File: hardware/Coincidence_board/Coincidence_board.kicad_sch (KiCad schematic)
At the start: 68 parts, among them J1 Inputs, J3 POWER_IN, J4 Morpho_Gauche, J7 Morpho_Droite, SW1 SW_1, U1 74HCT74, U2 74HCT74, U3 LM7805_TO220, U4 74HC74, U5 74HC74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

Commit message: Update Coincidence Board / Dephi 2024
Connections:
- net A2out_nuc: now also J7.29 (Pin_29); no longer J7.5 (Pin_5)
- net AB2out_nuc: now also J7.5 (Pin_5); no longer J7.32 (Pin_32)
- net ABCout_nuc: now also J7.33 (Pin_33); no longer J7.13 (Pin_13)
- net AC2out_nuc: now also J4.37 (Pin_37); no longer J7.26 (Pin_26)
- net B2out_nuc: now also J4.15 (Pin_15); no longer J7.7 (Pin_7)
- net BC2out_nuc: now also J4.3 (Pin_3); no longer J7.31 (Pin_31)
- net C2out_nuc: now also J4.40 (Pin_40)
- net GND: now also U1.2 (D)
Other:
- note added: "PB_4"
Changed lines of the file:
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@@
 	(wire
 		(pts
+			(xy 90.17 185.42) (xy 91.44 185.42)
+		)
+		(stroke
+			(width 0)
+			(type default)
+		)
+	)
+	(wire
+		(pts
 			(xy 49.53 170.18) (xy 52.07 170.18)
 		)
@@
 	(wire
 		(pts
+			(xy 90.17 180.34) (xy 91.44 180.34)
+		)
+		(stroke
+			(width 0)
+			(type default)
+		)
+	)
+	(wire
+		(pts
 			(xy 68.58 73.66) (xy 68.58 74.93)
 		)
@@
 	(wire
 		(pts
+			(xy 128.27 30.48) (xy 130.81 30.48)
+		)
+		(stroke
+			(width 0)
+			(type default)
+		)
+	)
+	(wire
+		(pts
 			(xy 264.16 83.82) (xy 265.43 83.82)
 		)
@@
 	(text "PB_8"
 		(exclude_from_sim no)
-		(at 75.692 149.86 0)
+		(at 74.168 150.114 0)
 		(effects
 			(font
@@
 	(text "PB_0"
 		(exclude_from_sim no)
-		(at 70.866 188.214 0)
+		(at 64.77 187.706 0)
 		(effects
 			(font
@@
 	(text "PB_9"
 		(exclude_from_sim no)
-		(at 75.692 152.654 0)
+		(at 74.168 152.654 0)
 		(effects
 			(font
@@
 	(text "PC_1"
 		(exclude_from_sim no)
-		(at 70.866 191.008 0)
+		(at 64.77 190.5 0)
 		(effects
 			(font
@@
 	(text "PC_0"
 		(exclude_from_sim no)
-		(at 70.866 193.548 0)
+		(at 64.77 193.04 0)
 		(effects
 			(font
@@
 		)
 	)
+	(text "PB_4"
+		(exclude_from_sim no)
+		(at 73.914 180.594 0)
+		(effects
+			(font
+				(size 1.27 1.27)
+			)
+		)
+	)
 	(text "PA_0"
 		(exclude_from_sim no)
@@
 	(global_label "C2out_nuc"
 		(shape input)
-		(at 105.41 160.02 0)
+		(at 49.53 193.04 0)
 		(fields_autoplaced yes)
 		(effects
@@
 		)
 		(property "Intersheetrefs" "${INTERSHEET_REFS}"
-			(at 117.5984 160.02 0)
+			(at 61.7184 193.04 0)
 			(effects
 				(font
@@
 	(global_label "BC2out_nuc"
 		(shape input)
-		(at 90.17 182.88 180)
+		(at 36.83 147.32 180)
 		(fields_autoplaced yes)
 		(effects
@@
 		)
 		(property "Intersheetrefs" "${INTERSHEET_REFS}"
-			(at 76.7116 182.88 0)
+			(at 23.3716 147.32 0)
 			(effects
 				(font
@@
 	(global_label "ABCout_nuc"
 		(shape input)
-		(at 90.17 160.02 180)
+		(at 90.17 185.42 180)
 		(fields_autoplaced yes)
 		(effects
@@
 		)
 		(property "Intersheetrefs" "${INTERSHEET_REFS}"
-			(at 76.8325 160.02 0)
+			(at 76.8325 185.42 0)
 			(effects
 				(font
@@
 	(global_label "AB2out_nuc"
 		(shape input)
-		(at 105.41 182.88 0)
+		(at 90.17 149.86 180)
 		(fields_autoplaced yes)
 		(effects
@@
 				(size 1.27 1.27)
 			)
-			(justify left)
+			(justify right)
 		)
 		(property "Intersheetrefs" "${INTERSHEET_REFS}"
-			(at 118.687 182.88 0)
+			(at 76.893 149.86 0)
 			(effects
 				(font
 					(size 1.27 1.27)
 				)
-				(justify left)
+				(justify right)
 				(hide yes)
 			)
@@
 	(global_label "B2out_nuc"
 		(shape input)
-		(at 90.17 152.4 180)
+		(at 36.83 162.56 180)
 		(fields_autoplaced yes)
 		(effects
@@
 		)
 		(property "Intersheetrefs" "${INTERSHEET_REFS}"
-			(at 77.9816 152.4 0)
+			(at 24.6416 162.56 0)
 			(effects
 				(font
@@
 	(global_label "A2out_nuc"
 		(shape input)
-		(at 90.17 149.86 180)
+		(at 90.17 180.34 180)
 		(fields_autoplaced yes)
 		(effects
@@
 		)
 		(property "Intersheetrefs" "${INTERSHEET_REFS}"
-			(at 78.163 149.86 0)
+			(at 78.163 180.34 0)
 			(effects
 				(font
@@
 	(global_label "AC2out_nuc"
 		(shape input)
-		(at 105.41 175.26 0)
+		(at 36.83 190.5 180)
 		(fields_autoplaced yes)
 		(effects
@@
 				(size 1.27 1.27)
 			)
-			(justify left)
+			(justify right)
 		)
 		(property "Intersheetrefs" "${INTERSHEET_REFS}"
-			(at 118.687 175.26 0)
+			(at 23.553 190.5 0)
 			(effects
 				(font
 					(size 1.27 1.27)
 				)
-				(justify left)
+				(justify right)
 				(hide yes)
 			)

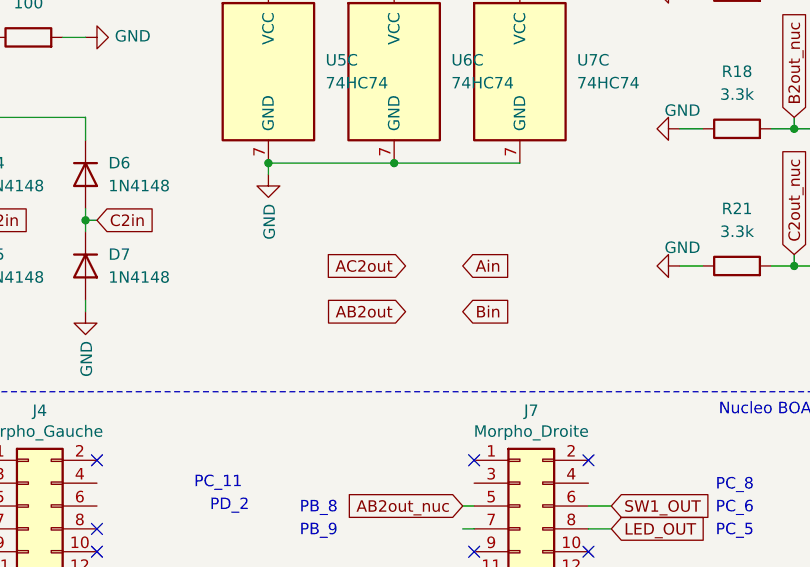
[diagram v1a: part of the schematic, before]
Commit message: Update Schematics of Electronic Board
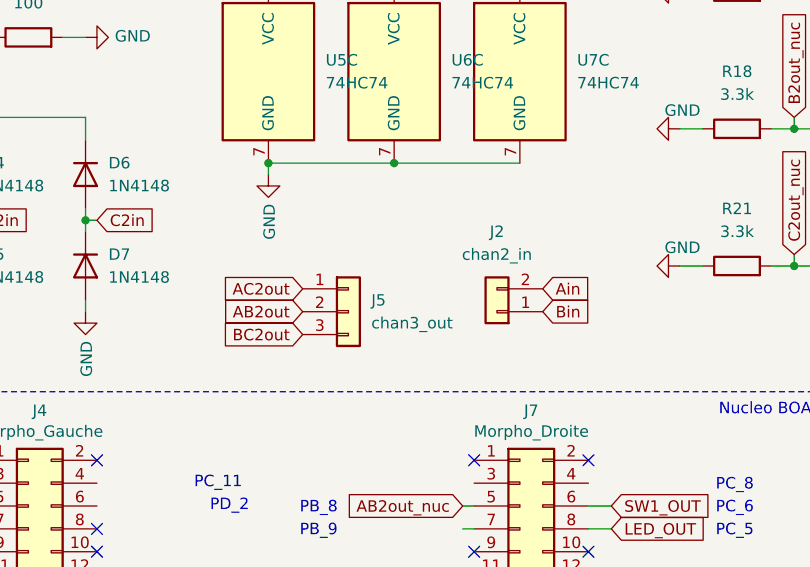
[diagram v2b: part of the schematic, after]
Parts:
- added J2: chan2_in, Connector_PinHeader_2.54mm:PinHeader_1x02_P2.54mm_Vertical, symbol Connector_Generic:Conn_01x02
- added J5: chan3_out, Connector_PinHeader_2.54mm:PinHeader_1x03_P2.54mm_Vertical, symbol Connector_Generic:Conn_01x03
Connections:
- net AB2out: now also J5.2 (Pin_2)
- net AC2out: now also J5.1 (Pin_1)
- net Ain: now also J2.2 (Pin_2)
- net BC2out: now also J5.3 (Pin_3)
- net Bin: now also J2.1 (Pin_1)
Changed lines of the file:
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@@
 	(global_label "Ain"
 		(shape input)
-		(at 90.17 123.19 0)
+		(at 99.06 125.73 0)
 		(fields_autoplaced yes)
 		(effects
@@
 		)
 		(property "Intersheetrefs" "${INTERSHEET_REFS}"
-			(at 95.3434 123.19 0)
+			(at 104.2334 125.73 0)
 			(effects
 				(font
@@
 	(global_label "AB2out"
 		(shape input)
-		(at 83.82 128.27 180)
+		(at 72.39 128.27 180)
 		(fields_autoplaced yes)
 		(effects
@@
 		)
 		(property "Intersheetrefs" "${INTERSHEET_REFS}"
-			(at 74.8972 128.27 0)
+			(at 63.4672 128.27 0)
 			(effects
 				(font
@@
 	(global_label "Bin"
 		(shape input)
-		(at 90.17 128.27 0)
+		(at 99.06 128.27 0)
 		(fields_autoplaced yes)
 		(effects
@@
 		)
 		(property "Intersheetrefs" "${INTERSHEET_REFS}"
-			(at 95.5248 128.27 0)
+			(at 104.4148 128.27 0)
 			(effects
 				(font
@@
 		)
 	)
+	(global_label "BC2out"
+		(shape input)
+		(at 72.39 130.81 180)
+		(fields_autoplaced yes)
+		(effects
+			(font
+				(size 1.27 1.27)
+			)
+			(justify right)
+		)
+		(property "Intersheetrefs" "${INTERSHEET_REFS}"
+			(at 63.2858 130.81 0)
+			(effects
+				(font
+					(size 1.27 1.27)
+				)
+				(justify right)
+				(hide yes)
+			)
+		)
+	)
 	(global_label "5V"
 		(shape input)
@@
 	(global_label "AC2out"
 		(shape input)
-		(at 83.82 123.19 180)
+		(at 72.39 125.73 180)
 		(fields_autoplaced yes)
 		(effects
@@
 		)
 		(property "Intersheetrefs" "${INTERSHEET_REFS}"
-			(at 74.8972 123.19 0)
+			(at 63.4672 125.73 0)
 			(effects
 				(font
@@
 	)
 	(symbol
+		(lib_id "Connector_Generic:Conn_01x02")
+		(at 93.98 128.27 180)
+		(unit 1)
+		(exclude_from_sim no)
+		(in_bom yes)
+		(on_board yes)
+		(dnp no)
+		(fields_autoplaced yes)
+		(property "Reference" "J2"
+			(at 93.98 119.38 0)
+			(effects
+				(font
+					(size 1.27 1.27)
+				)
+			)
+		)
+		(property "Value" "chan2_in"
+			(at 93.98 121.92 0)
+			(effects
+				(font
+					(size 1.27 1.27)
+				)
+			)
+		)
+		(property "Footprint" "Connector_PinHeader_2.54mm:PinHeader_1x02_P2.54mm_Vertical"
+			(at 93.98 128.27 0)
+			(effects
+				(font
+					(size 1.27 1.27)
+				)
+				(hide yes)
+			)
+		)
+		(property "Datasheet" "~"
+			(at 93.98 128.27 0)
+			(effects
+				(font
+					(size 1.27 1.27)
+				)
+				(hide yes)
+			)
+		)
+		(property "Description" "Generic connector, single row, 01x02, script generated (kicad-library-utils/schlib/autogen/connector/)"
+			(at 93.98 128.27 0)
+			(effects
+				(font
+					(size 1.27 1.27)
+				)
+				(hide yes)
+			)
+		)
+		(pin "1"
+		)
+		(pin "2"
+		)
+		(instances
+			(project "Coincidence_board"
+				(path "/44ad8000-4ee7-4966-8fe6-195894dfb602"
+					(reference "J2")
+					(unit 1)
+				)
+			)
+		)
+	)
+	(symbol
 		(lib_id "Device:C")
 		(at 71.12 36.83 0)
@@
 					(unit 1)
 				)
+			)
+		)
+	)
+	(symbol
+		(lib_id "Connector_Generic:Conn_01x03")
+		(at 77.47 128.27 0)
+		(unit 1)
+		(exclude_from_sim no)
+		(in_bom yes)
+		(on_board yes)
+		(dnp no)
+		(fields_autoplaced yes)
+		(property "Reference" "J5"
+			(at 80.01 126.9999 0)
+			(effects
+				(font
+					(size 1.27 1.27)
+				)
+				(justify left)
+			)
+		)
+		(property "Value" "chan3_out"
+			(at 80.01 129.5399 0)
+			(effects
+				(font
+					(size 1.27 1.27)
+				)
+				(justify left)
+			)
+		)
+		(property "Footprint" "Connector_PinHeader_2.54mm:PinHeader_1x03_P2.54mm_Vertical"
+			(at 77.47 128.27 0)
+			(effects
+				(font
+					(size 1.27 1.27)
+				)
+				(hide yes)
+			)
+		)
+		(property "Datasheet" "~"
+			(at 77.47 128.27 0)
+			(effects
+				(font
+					(size 1.27 1.27)
+				)
+				(hide yes)
+			)
+		)
+		(property "Description" "Generic connector, single row, 01x03, script generated (kicad-library-utils/schlib/autogen/connector/)"
+			(at 77.47 128.27 0)
+			(effects
+				(font
+					(size 1.27 1.27)
+				)
+				(hide yes)
+			)
+		)
+		(pin "3"
+		)
+		(pin "1"
+		)
+		(pin "2"
+		)
+		(instances
+			(project "Coincidence_board"
+				(path "/44ad8000-4ee7-4966-8fe6-195894dfb602"
+					(reference "J5")
+					(unit 1)
+				)

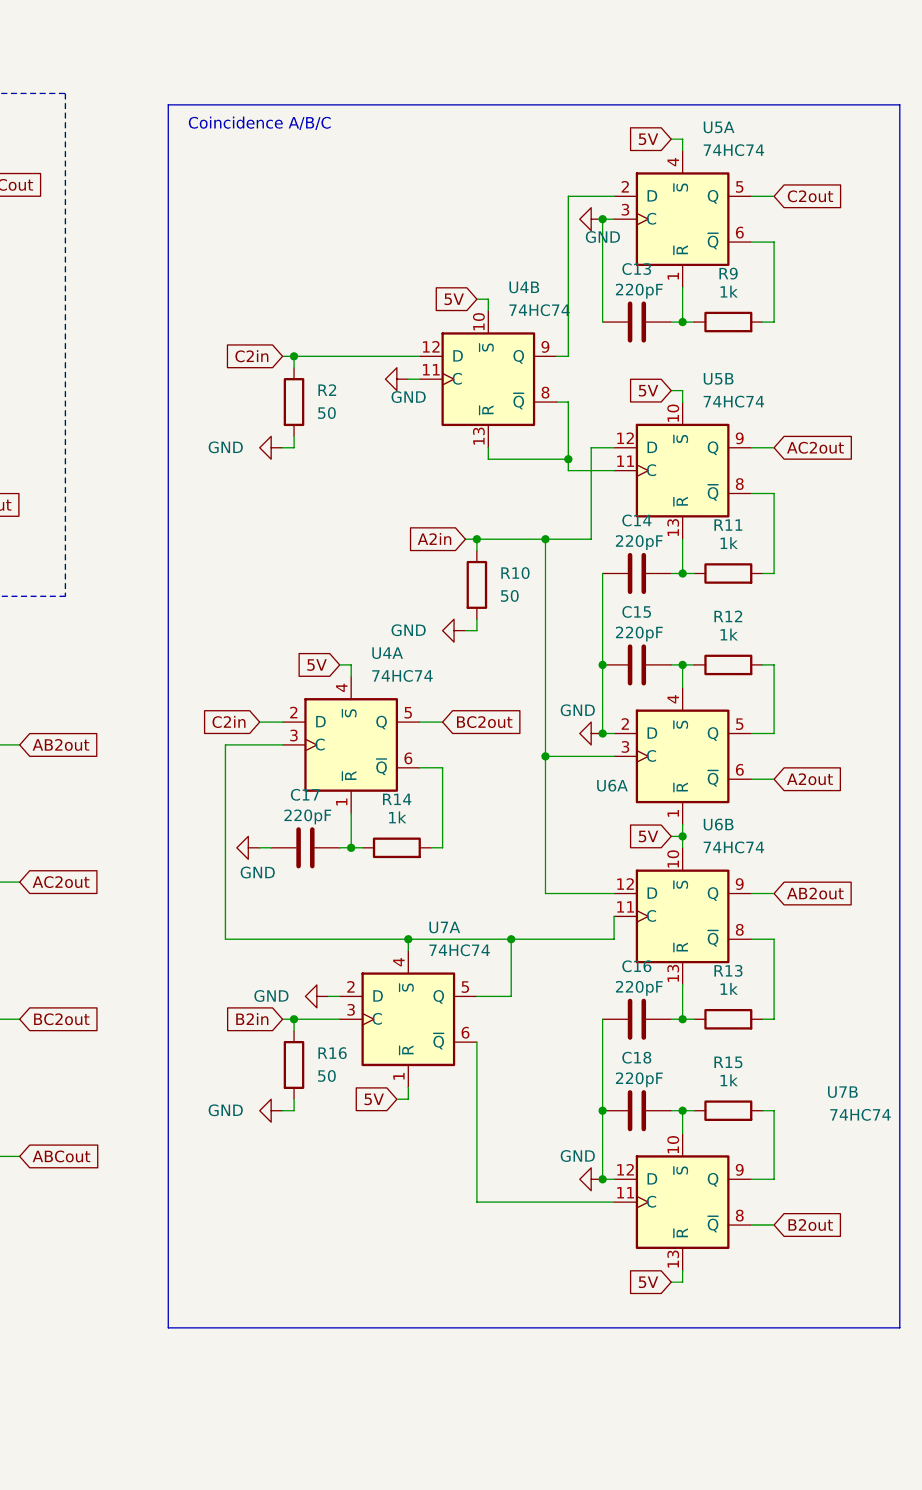
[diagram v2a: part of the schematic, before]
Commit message: Update Coincidence Board / New schematics (Anouk - Jeanne)
Test with Nucleo L476RG ? Not fast enough ??
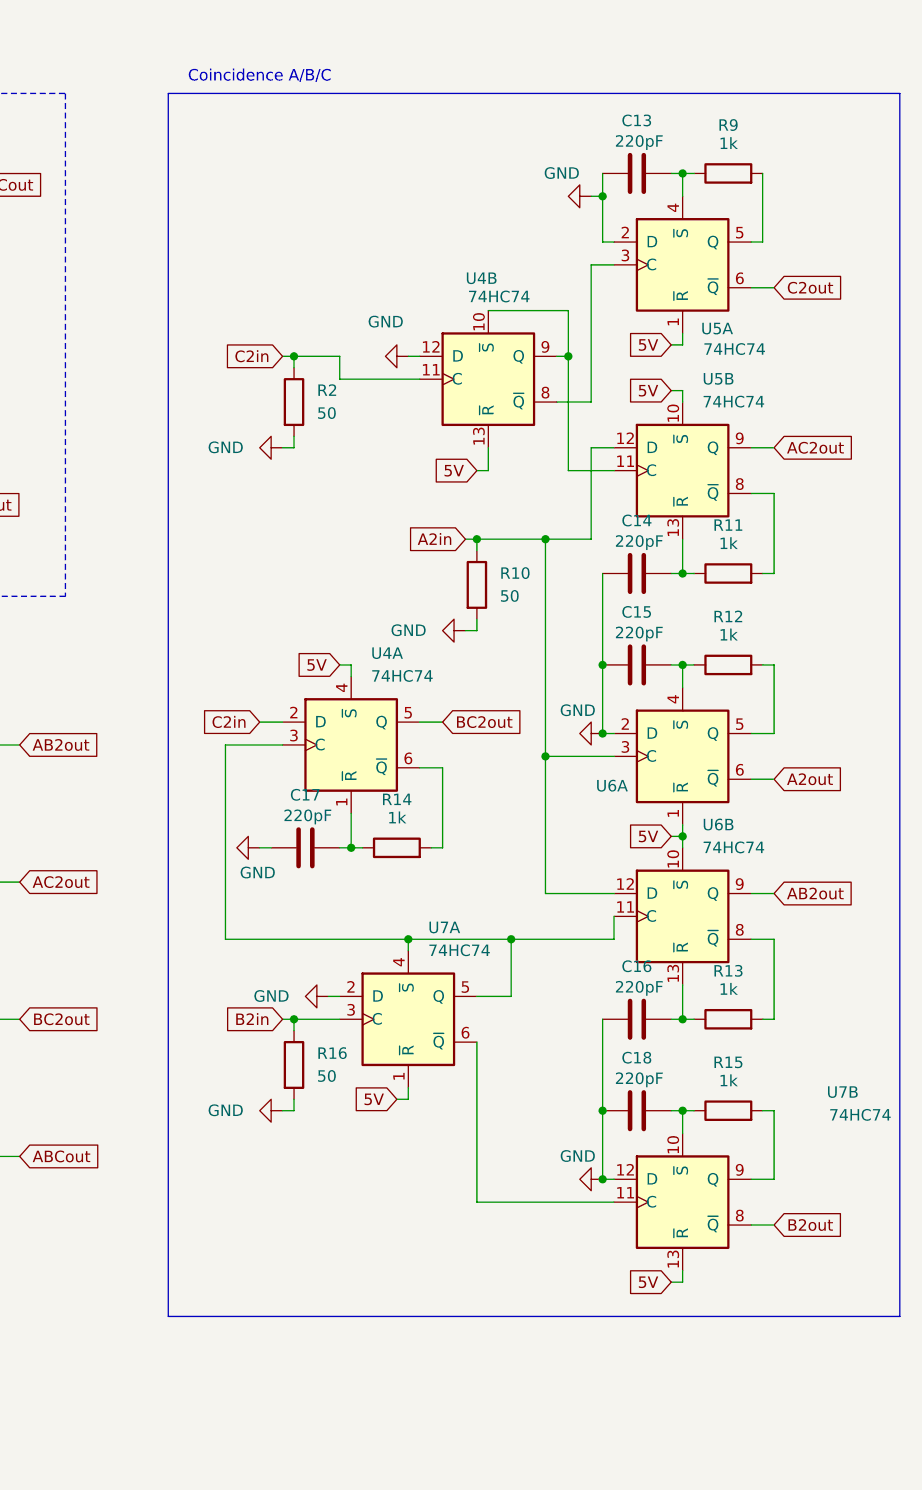
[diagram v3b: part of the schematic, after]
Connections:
- net 5V: now also U4.13 (~{R}), U5.1 (~{R}); no longer U4.10 (~{S}), U5.4 (~{S})
- net C2in: now also U4.11 (C); no longer U4.12 (D)
- net C2out: now also U5.6 (~{Q}); no longer U5.5 (Q)
- net GND: now also U4.12 (D), U5.2 (D); no longer U4.11 (C), U5.3 (C)
- net at C13.2, R9.1: now also U5.4 (~{S}); no longer U5.1 (~{R})
- net at R9.2: now also U5.5 (Q); no longer U5.6 (~{Q})
- net at U4.9 (Q): now also U4.10 (~{S}), U5.11 (C); no longer U5.2 (D)
- new net: U4.8 (~{Q}), U5.3 (C)
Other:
- moved on the sheet: C13, R9, U5A
